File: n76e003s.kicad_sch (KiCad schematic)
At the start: 16 parts, among them J1 Conn_02x07_Counter_Clockwise, J2 Conn_02x07_Counter_Clockwise, J3 Conn_02x07_Counter_Clockwise, J4 Conn_02x06_Counter_Clockwise, J5 Conn_02x07_Counter_Clockwise, J7 Conn_02x07_Counter_Clockwise, U3 N76E003AQ20, U4 N76E003AQ20, U5 N76E003AQ20, U6 N76E003AQ20

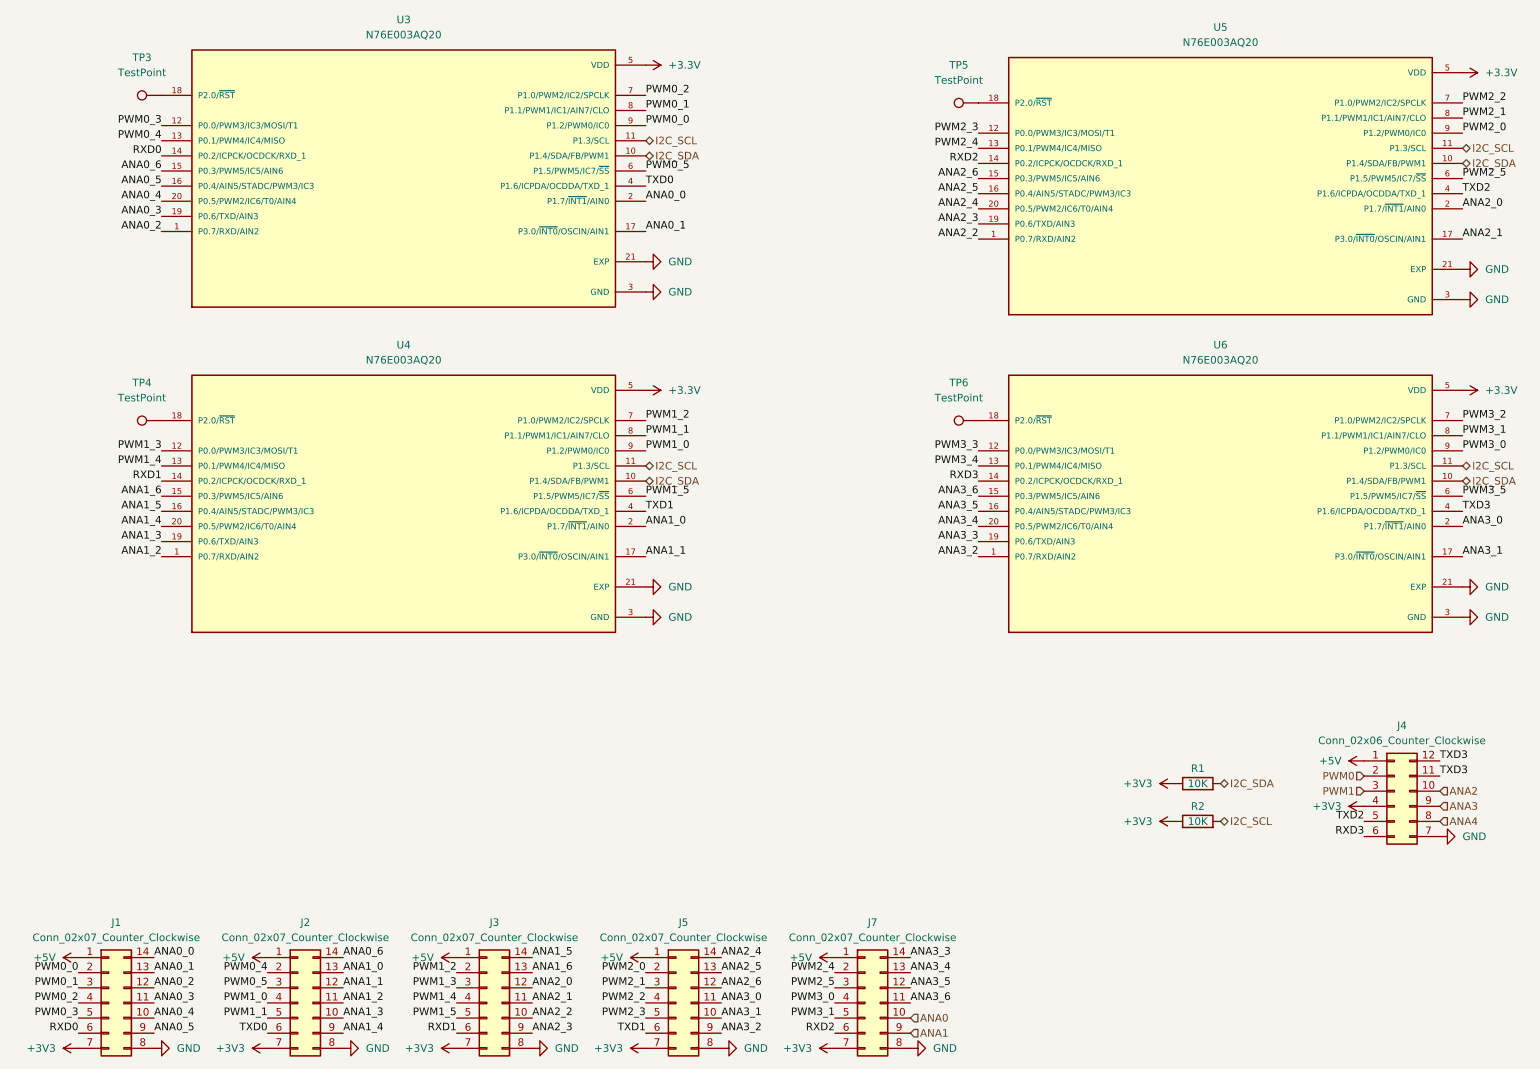
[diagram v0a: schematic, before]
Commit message: redesigned everything x)
new BMS design, switched to ESP32-S3 with external antenna, implement USB-C PD, add analog mux, add PWM controller, add USB to serial
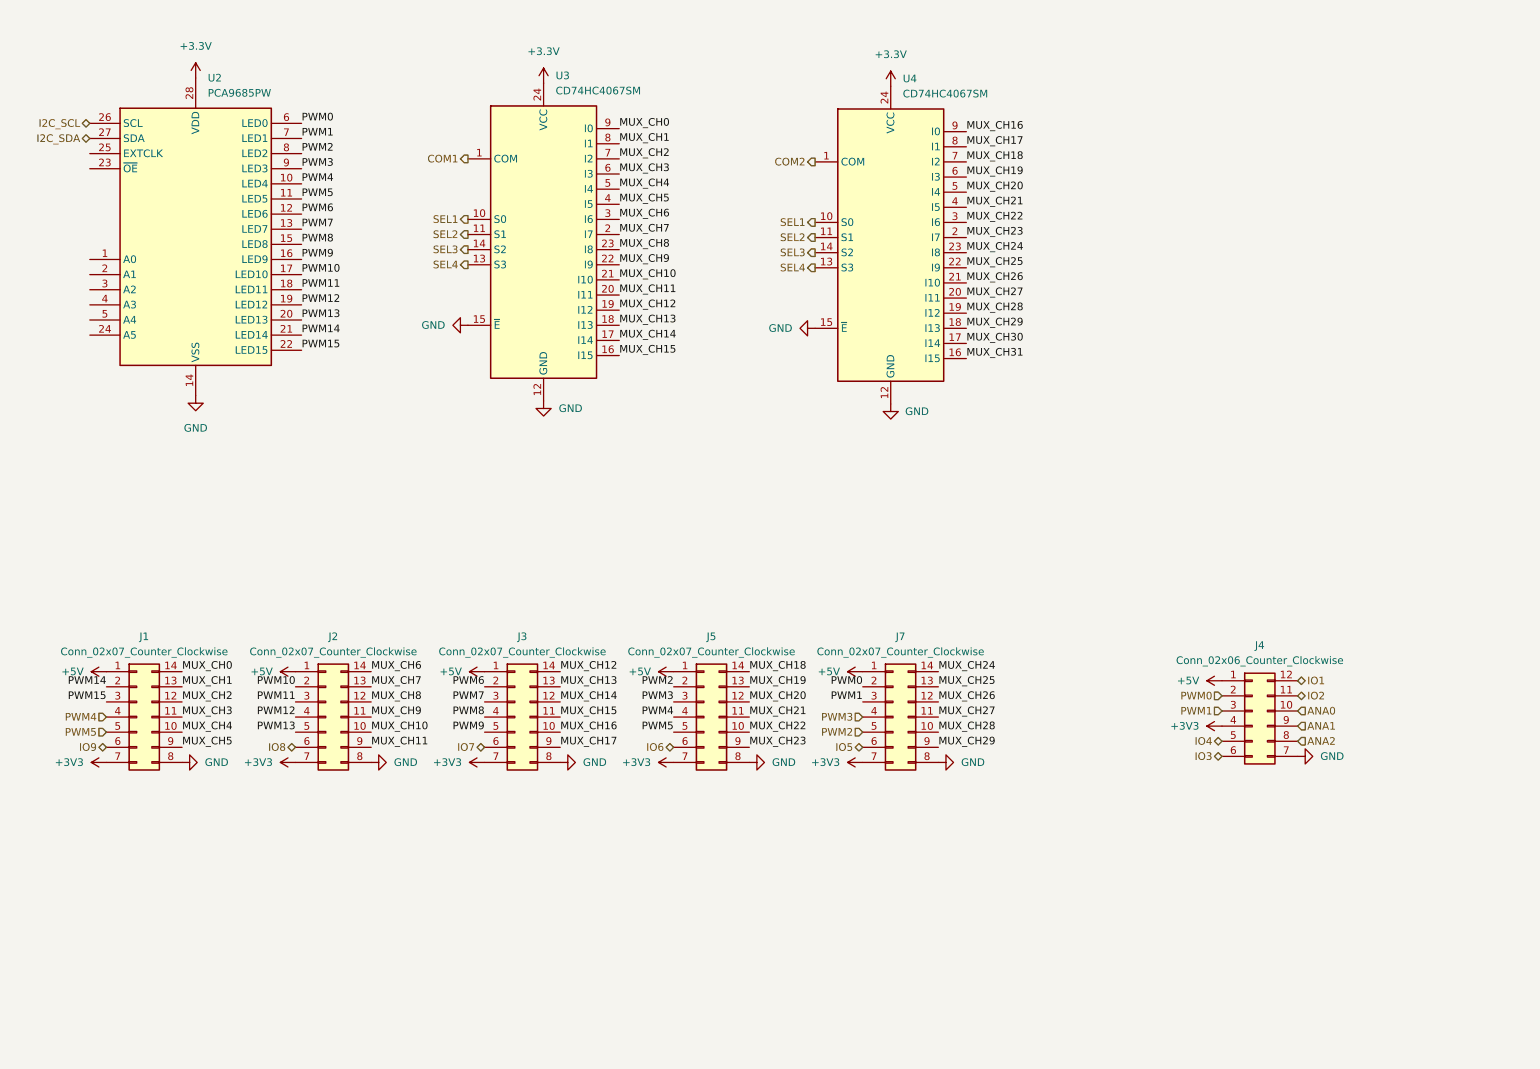
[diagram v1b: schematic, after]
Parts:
- removed R1, R2: 10K, Resistor_SMD:R_0201_0603Metric, symbol Device:R
- removed TP3, TP4, TP5, TP6: TestPoint, TestPoint:TestPoint_Pad_D1.5mm, symbol Connector:TestPoint
- removed U3, U4, U5, U6: N76E003AQ20, Footprint:QFN40P300X300X80-21N, symbol N76E003AQ20:N76E003AQ20
- added U2: PCA9685PW, Package_SO:TSSOP-28_4.4x9.7mm_P0.65mm, symbol Driver_LED:PCA9685PW
- added U3, U4: CD74HC4067SM, Package_SO:SSOP-24_5.3x8.2mm_P0.65mm, symbol 74xx:CD74HC4067SM
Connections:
- net ANA3 is gone; now on net ANA1: J4.9 (Pin_9)
- net ANA4 is gone; now on net ANA2: J4.8 (Pin_8)
- net PWM2_2 is gone; now on net PWM4: J5.4 (Pin_4)
- net PWM2_3 is gone; now on net PWM5: J5.5 (Pin_5)
- net PWM2_4 is gone; now on net PWM0: J7.2 (Pin_2)
- net PWM2_5 is gone; now on net PWM1: J7.3 (Pin_3)
- net PWM3_0 is gone; now on net PWM3: J7.4 (Pin_4)
- net PWM3_1 is gone; now on net PWM2: J7.5 (Pin_5)
- net ANA0: now also J4.10 (Pin_10); no longer J7.10 (Pin_10)
- net ANA1: no longer J7.9 (Pin_9)
- net ANA2: no longer J4.10 (Pin_10)
- net GND: now also U2.14 (VSS), U3.12 (GND), U3.15 (~{E}), U4.12 (GND), U4.15 (~{E})
- net I2C_SCL: now also U2.26 (SCL)
- net I2C_SDA: now also U2.27 (SDA)
- net PWM0: now also U2.6 (LED0)
- net PWM1: now also U2.7 (LED1)
- net ANA0_0 renamed MUX_CH0
- net MUX_CH0: now also U3.9 (I0)
- net ANA0_1 renamed MUX_CH1
- net MUX_CH1: now also U3.8 (I1)
- net ANA0_2 renamed MUX_CH2
- net MUX_CH2: now also U3.7 (I2)
- net ANA0_3 renamed MUX_CH3
- net MUX_CH3: now also U3.6 (I3)
- net ANA0_4 renamed MUX_CH4
- net MUX_CH4: now also U3.5 (I4)
- net ANA0_5 renamed MUX_CH5
- net MUX_CH5: now also U3.4 (I5)
- net ANA0_6 renamed MUX_CH6
- net MUX_CH6: now also U3.3 (I6)
- net ANA1_0 renamed MUX_CH7
- net MUX_CH7: now also U3.2 (I7)
- net ANA1_1 renamed MUX_CH8
- net MUX_CH8: now also U3.23 (I8)
- net ANA1_2 renamed MUX_CH9
- net MUX_CH9: now also U3.22 (I9)
- net ANA1_3 renamed MUX_CH10
- net MUX_CH10: now also U3.21 (I10)
- net ANA1_4 renamed MUX_CH11
- net MUX_CH11: now also U3.20 (I11)
- net ANA1_5 renamed MUX_CH12
- net MUX_CH12: now also U3.19 (I12)
- net ANA1_6 renamed MUX_CH13
- net MUX_CH13: now also U3.18 (I13)
- net ANA2_0 renamed MUX_CH14
- net MUX_CH14: now also U3.17 (I14)
- net ANA2_1 renamed MUX_CH15
- net MUX_CH15: now also U3.16 (I15)
- net ANA2_2 renamed MUX_CH16
- net MUX_CH16: now also U4.9 (I0)
- net ANA2_3 renamed MUX_CH17
- net MUX_CH17: now also U4.8 (I1)
- net ANA2_4 renamed MUX_CH18
- net MUX_CH18: now also U4.7 (I2)
- net ANA2_5 renamed MUX_CH19
- net MUX_CH19: now also U4.6 (I3)
- net ANA2_6 renamed MUX_CH20
- net MUX_CH20: now also U4.5 (I4)
- net ANA3_0 renamed MUX_CH21
- net MUX_CH21: now also U4.4 (I5)
- net ANA3_1 renamed MUX_CH22
- net MUX_CH22: now also U4.3 (I6)
- net ANA3_2 renamed MUX_CH23
- net MUX_CH23: now also U4.2 (I7)
- net ANA3_3 renamed MUX_CH24
- net MUX_CH24: now also U4.23 (I8)
- net ANA3_4 renamed MUX_CH25
- net MUX_CH25: now also U4.22 (I9)
- net ANA3_5 renamed MUX_CH26
- net MUX_CH26: now also U4.21 (I10)
- net ANA3_6 renamed MUX_CH27
- net MUX_CH27: now also U4.20 (I11)
- net PWM0_0 renamed PWM14
- net PWM14: now also U2.21 (LED14)
- net PWM0_1 renamed PWM15
- net PWM15: now also U2.22 (LED15)
- net PWM0_2 renamed PWM4
- net PWM4: now also U2.10 (LED4)
- net PWM0_3 renamed PWM5
- net PWM5: now also U2.11 (LED5)
- net PWM0_4 renamed PWM10
- net PWM10: now also U2.17 (LED10)
- net PWM0_5 renamed PWM11
- net PWM11: now also U2.18 (LED11)
- net PWM1_0 renamed PWM12
- net PWM12: now also U2.19 (LED12)
- net PWM1_1 renamed PWM13
- net PWM13: now also U2.20 (LED13)
- net PWM1_2 renamed PWM6
- net PWM6: now also U2.12 (LED6)
- net PWM1_3 renamed PWM7
- net PWM7: now also U2.13 (LED7)
- net PWM1_4 renamed PWM8
- net PWM8: now also U2.15 (LED8)
- net PWM1_5 renamed PWM9
- net PWM9: now also U2.16 (LED9)
- net PWM2_0 renamed PWM2
- net PWM2: now also U2.8 (LED2)
- net PWM2_1 renamed PWM3
- net PWM3: now also U2.9 (LED3)
- net RXD0 renamed IO9
- net RXD1 renamed IO7
- net RXD2 renamed IO5
- net RXD3 renamed IO3
- net TXD0 renamed IO8
- net TXD1 renamed IO6
- net TXD2 renamed IO4
- net TXD3 renamed IO1
- net IO1: no longer J4.11 (Pin_11)
- new net +3.3V: U2.28 (VDD), U3.24 (VCC), U4.24 (VCC)
- new net COM1: U3.1 (COM)
- new net COM2: U4.1 (COM)
- new net IO2: J4.11 (Pin_11)
- new net MUX_CH28: J7.10 (Pin_10), U4.19 (I12)
- new net MUX_CH29: J7.9 (Pin_9), U4.18 (I13)
- new net MUX_CH30: U4.17 (I14)
- new net MUX_CH31: U4.16 (I15)
- new net SEL1: U3.10 (S0), U4.10 (S0)
- new net SEL2: U3.11 (S1), U4.11 (S1)
- new net SEL3: U3.14 (S2), U4.14 (S2)
- new net SEL4: U3.13 (S3), U4.13 (S3)
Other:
- moved on the sheet: J1, J2, J3, J4, J5, J7
